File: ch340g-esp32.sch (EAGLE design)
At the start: 0 parts

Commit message: rev1
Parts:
- added C1, C2: 22, rcl:C-EUC0805
- added C3, C5: 0.1uF, rcl:C-EUC0805
- added C4: 10uF, rcl:CPOL-EUB/3528-21W
- added D1: YELLOW, 597-5311-402F:597-5311-402F
- added D2: GREEN, 597-5311-402F:597-5311-402F
- added IC1: LM1117MPX-3.3, lm1117:LM1117MPX-3.3
- added JP1: OUT, pinhead:PINHD-1X6
- added Q1: 12M, crystal:CRYSTALHC49S
- added R1, R2: 10K, rcl:R-EU_R0805
- added R3, R4: 2K, rcl:R-EU_R0805
- added T1, T2: BC847, transistor:BC847
- added U$1: MICRO-USB, microusb:MICRO-USB
- added U$2: CH340G, ch340g:CH340G
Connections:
- new net +5V: C3.1, IC1.IN, U$1.VCC
- new net D+: U$1.D+, U$2.D+
- new net D-: U$1.D-, U$2.D-
- new net DTR: R1.1, T2.E, U$2.DTR
- new net EN: JP1.1, T1.C
- new net GND: C1.2, C2.2, C3.2, C4.-, C5.2, IC1.GND, JP1.6, U$1.GND, U$1.GND@1, U$1.GND@2, U$2.GND
- new net IO0: JP1.2, T2.C
- new net N$1: C2.1, Q1.2, U$2.XO
- new net N$12: D2.A, R4.1
- new net N$2: C1.1, Q1.1, U$2.XI
- new net N$3: R1.2, T1.B
- new net N$4: R2.2, T2.B
- new net N$5: D1.A, R3.1
- new net RTS: R2.1, T1.E, U$2.RTS
- new net RX: D2.C, JP1.3, U$2.RX
- new net TX: D1.C, JP1.4, U$2.TX
- new net VCC: C4.+, C5.1, IC1.OUT, IC1.OUT1, JP1.5, R3.2, R4.2, U$2.V3, U$2.VCC

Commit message: board update
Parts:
- added D3: GREEN, 597-5311-402F:597-5311-402F
- added R5: 2K, rcl:R-EU_R0805
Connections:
- new net N$6: D3.A, R5.1
- net GND: now also D3.C
- net VCC: now also R5.2
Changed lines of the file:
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@@
 <?xml version="1.0" encoding="utf-8"?>
 <!DOCTYPE eagle SYSTEM "eagle.dtd">
-<eagle version="9.4.2">
+<eagle version="9.5.0">
 <drawing>
 <settings>
@@
 <part name="P+9" library="supply1" library_urn="urn:adsk.eagle:library:371" deviceset="VCC" device=""/>
 <part name="GND10" library="supply1" library_urn="urn:adsk.eagle:library:371" deviceset="GND" device=""/>
+<part name="D3" library="597-5311-402F" deviceset="597-5311-402F" device="" value="GREEN"/>
+<part name="R5" library="rcl" library_urn="urn:adsk.eagle:library:334" deviceset="R-EU_" device="R0805" package3d_urn="urn:adsk.eagle:package:23553/2" value="2K"/>
+<part name="P+10" library="supply1" library_urn="urn:adsk.eagle:library:371" deviceset="VCC" device=""/>
+<part name="GND11" library="supply1" library_urn="urn:adsk.eagle:library:371" deviceset="GND" device=""/>
 </parts>
 <sheets>
@@
 <attribute name="VALUE" x="7.62" y="-5.08" size="1.778" layer="96"/>
 </instance>
+<instance part="D3" gate="G$1" x="106.68" y="2.54" smashed="yes" rot="R90">
+<attribute name="NAME" x="102.60973125" y="0.50486875" size="1.780740625" layer="95" rot="R90"/>
+<attribute name="VALUE" x="110.49315" y="0.50631875" size="1.77946875" layer="96" rot="R90"/>
+</instance>
+<instance part="R5" gate="G$1" x="106.68" y="17.78" smashed="yes" rot="R90">
+<attribute name="NAME" x="105.1814" y="13.97" size="1.778" layer="95" rot="R90"/>
+<attribute name="VALUE" x="109.982" y="13.97" size="1.778" layer="96" rot="R90"/>
+</instance>
+<instance part="P+10" gate="VCC" x="106.68" y="25.4" smashed="yes">
+<attribute name="VALUE" x="104.14" y="22.86" size="1.778" layer="96" rot="R90"/>
+</instance>
+<instance part="GND11" gate="1" x="106.68" y="-7.62" smashed="yes">
+<attribute name="VALUE" x="104.14" y="-10.16" size="1.778" layer="96"/>
+</instance>
 </instances>
 <busses>
@@
 <pinref part="C4" gate="G$1" pin="-"/>
 <pinref part="GND10" gate="1" pin="GND"/>
+</segment>
+<segment>
+<pinref part="D3" gate="G$1" pin="C"/>
+<pinref part="GND11" gate="1" pin="GND"/>
 </segment>
 </net>
@@
 <junction x="20.32" y="58.42"/>
 </segment>
-</net>
+<segment>
+<pinref part="R5" gate="G$1" pin="2"/>
+<pinref part="P+10" gate="VCC" pin="VCC"/>
+</segment>
+</net>
+<net name="N$6" class="0">
+<segment>
+<pinref part="D3" gate="G$1" pin="A"/>
+<pinref part="R5" gate="G$1" pin="1"/>
+</segment>
+</net>

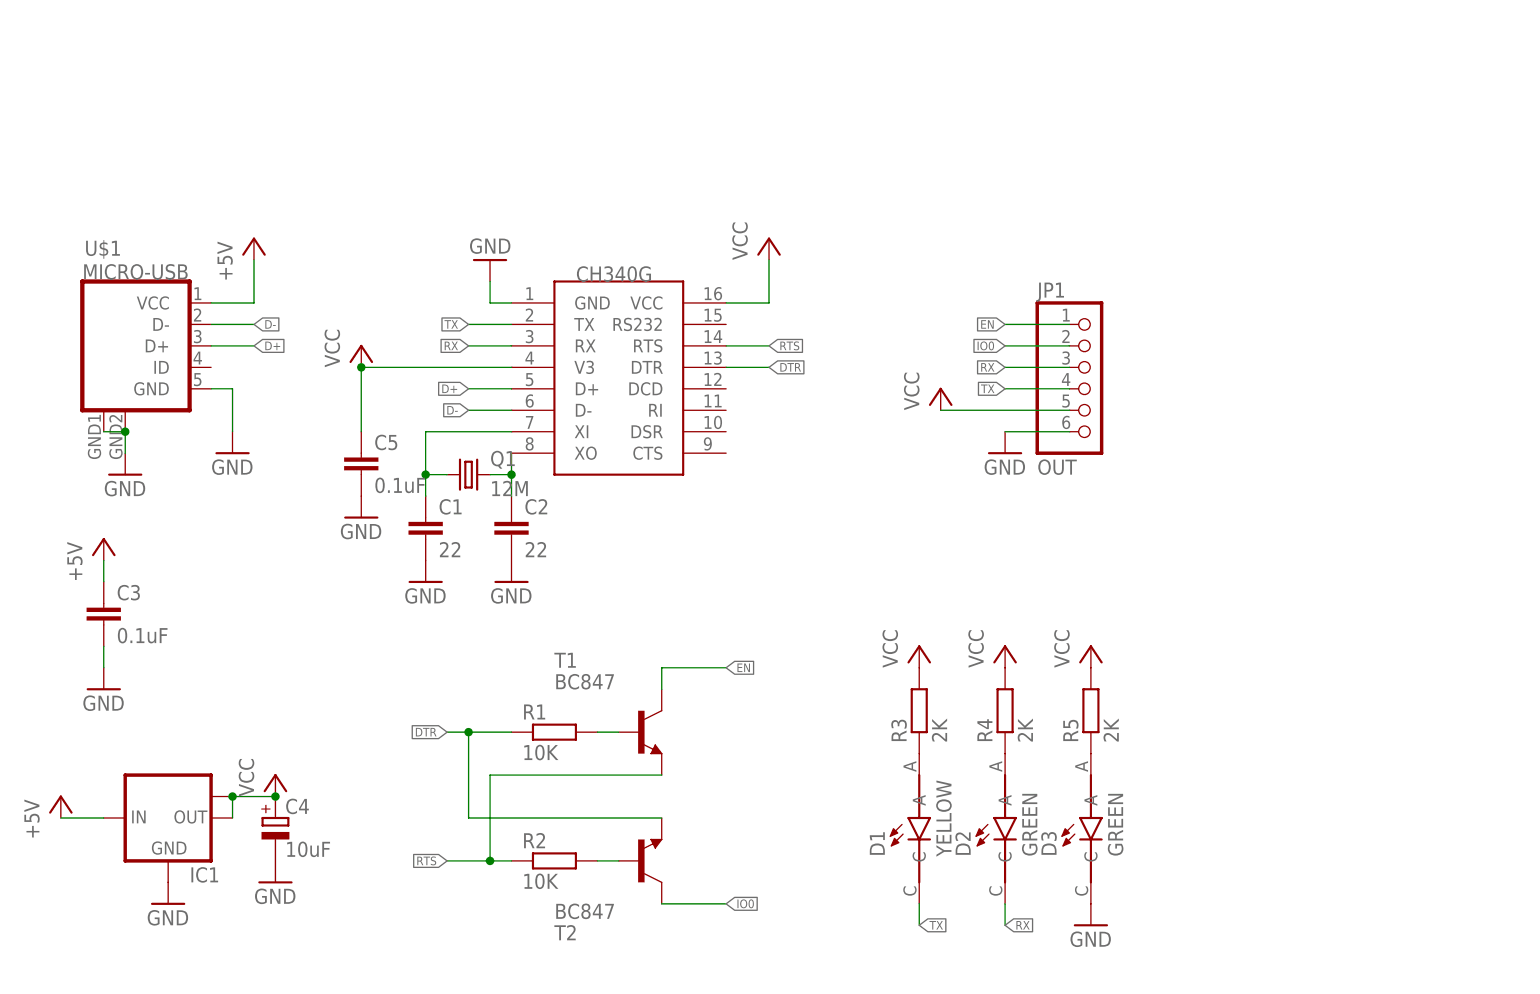
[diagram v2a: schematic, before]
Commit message: USB TypeC connector; Smaller board
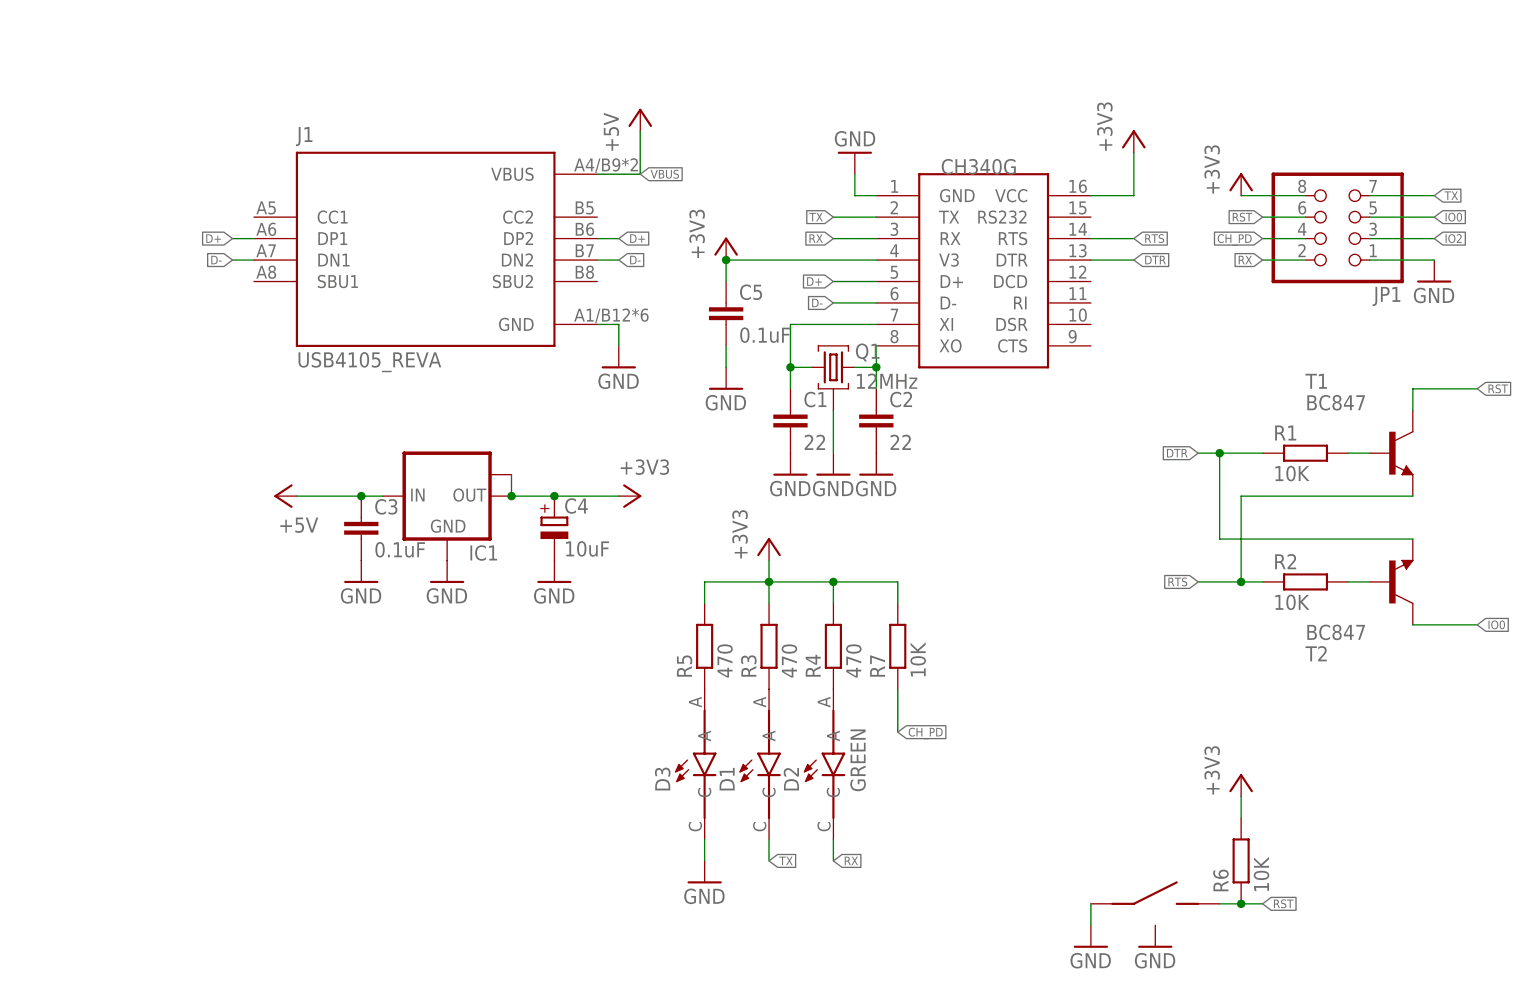
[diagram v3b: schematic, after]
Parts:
- removed U$2: CH340G, ch340g:CH340G
- added J1: USB4105_REVA, USB4105_REVA:USB4105_REVA
- added R6, R7: 10K, rcl:R-EU_R0603
- added U1: CH340G, ch340g:CH340G
- C1, C2, C3, C5: device rcl:C-EUC0805 -> rcl:C-EUC0603
- JP1: value OUT -> (none); device pinhead:PINHD-1X6 -> pinhead:PINHD-2X4
- Q1: value 12M -> 12MHz; device crystal:CRYSTALHC49S -> crystal:YSX321SL
- R1, R2: device rcl:R-EU_R0805 -> rcl:R-EU_R0603
- R3, R4, R5: value 2K -> 470; device rcl:R-EU_R0805 -> rcl:R-EU_R0603
- U$1: value MICRO-USB -> TS36CA-0.7; device microusb:MICRO-USB -> SMD Tact:TS36CA-0.7
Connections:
- removed net +5V: C3.1, IC1.IN, U$1.VCC
- removed net EN: JP1.1, T1.C
- removed net VCC: C4.+, C5.1, IC1.OUT, IC1.OUT1, JP1.5, R3.2, R4.2, R5.2, U$2.V3, U$2.VCC
- new net +3V3: C4.+, C5.1, IC1.OUT, IC1.OUT1, JP1.8, R3.2, R4.2, R5.2, R6.2, R7.2, U1.V3, U1.VCC
- new net CH_PD: JP1.4, R7.1
- new net IO2: JP1.3
- new net RST: JP1.6, R6.1, T1.C, U$1.P$2
- new net VBUS: C3.1, IC1.IN, J1.VBUS
- net D+: now also J1.DP1, J1.DP2, U1.D+; no longer U$1.D+, U$2.D+
- net D-: now also J1.DN1, J1.DN2, U1.D-; no longer U$1.D-, U$2.D-
- net DTR: now also U1.DTR; no longer U$2.DTR
- net GND: now also J1.GND, JP1.1, Q1.CASE, U$1.CASE, U$1.P$1, U1.GND; no longer JP1.6, U$1.GND, U$1.GND@1, U$1.GND@2, U$2.GND
- net IO0: now also JP1.5; no longer JP1.2
- net N$1: now also U1.XO; no longer U$2.XO
- net N$2: now also U1.XI; no longer U$2.XI
- net RTS: now also U1.RTS; no longer U$2.RTS
- net RX: now also JP1.2, U1.RX; no longer JP1.3, U$2.RX
- net TX: now also JP1.7, U1.TX; no longer JP1.4, U$2.TX
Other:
- moved on the sheet: C1, C2, C3, C4, C5, D1, D2, D3, IC1, R1, R2, R3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

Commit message: Production files
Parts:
- removed U$1: TS36CA-0.7, SMD Tact:TS36CA-0.7
- added BTN1: TS36CA-0.7, SMD Tact:TS36CA-0.7
- C3, C5: value 0.1uF -> 10u
- C4: value 10uF -> 100u
- D1: value YELLOW -> BLUE
- D2: value GREEN -> BLUE
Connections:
- net GND: now also BTN1.CASE, BTN1.P$1; no longer U$1.CASE, U$1.P$1
- net RST: now also BTN1.P$2; no longer U$1.P$2
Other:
- moved on the sheet: R6
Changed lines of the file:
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@@
 <part name="GND5" library="supply1" library_urn="urn:adsk.eagle:library:371" deviceset="GND" device=""/>
 <part name="R2" library="rcl" library_urn="urn:adsk.eagle:library:334" deviceset="R-EU_" device="R0603" package3d_urn="urn:adsk.eagle:package:23555/3" value="10K"/>
-<part name="D1" library="597-5311-402F" deviceset="597-5311-402F" device="" value="YELLOW"/>
-<part name="C3" library="rcl" library_urn="urn:adsk.eagle:library:334" deviceset="C-EU" device="C0603" package3d_urn="urn:adsk.eagle:package:23616/2" value="0.1uF"/>
+<part name="D1" library="597-5311-402F" deviceset="597-5311-402F" device="" value="BLUE"/>
+<part name="C3" library="rcl" library_urn="urn:adsk.eagle:library:334" deviceset="C-EU" device="C0603" package3d_urn="urn:adsk.eagle:package:23616/2" value="10u"/>
 <part name="GND6" library="supply1" library_urn="urn:adsk.eagle:library:371" deviceset="GND" device=""/>
-<part name="C4" library="rcl" library_urn="urn:adsk.eagle:library:334" deviceset="CPOL-EU" device="B/3528-21W" package3d_urn="urn:adsk.eagle:package:23411/1" value="10uF"/>
+<part name="C4" library="rcl" library_urn="urn:adsk.eagle:library:334" deviceset="CPOL-EU" device="B/3528-21W" package3d_urn="urn:adsk.eagle:package:23411/1" value="100u"/>
 <part name="GND7" library="supply1" library_urn="urn:adsk.eagle:library:371" deviceset="GND" device=""/>
 <part name="R3" library="rcl" library_urn="urn:adsk.eagle:library:334" deviceset="R-EU_" device="R0603" package3d_urn="urn:adsk.eagle:package:23555/3" value="470"/>
-<part name="C5" library="rcl" library_urn="urn:adsk.eagle:library:334" deviceset="C-EU" device="C0603" package3d_urn="urn:adsk.eagle:package:23616/2" value="0.1uF"/>
+<part name="C5" library="rcl" library_urn="urn:adsk.eagle:library:334" deviceset="C-EU" device="C0603" package3d_urn="urn:adsk.eagle:package:23616/2" value="10u"/>
 <part name="GND8" library="supply1" library_urn="urn:adsk.eagle:library:371" deviceset="GND" device=""/>
-<part name="D2" library="597-5311-402F" deviceset="597-5311-402F" device="" value="GREEN"/>
+<part name="D2" library="597-5311-402F" deviceset="597-5311-402F" device="" value="BLUE"/>
 <part name="R4" library="rcl" library_urn="urn:adsk.eagle:library:334" deviceset="R-EU_" device="R0603" package3d_urn="urn:adsk.eagle:package:23555/3" value="470"/>
 <part name="IC1" library="lm1117" deviceset="LM1117MPX-*" device="" technology="3.3" value=""/>
@@
 <part name="R7" library="rcl" library_urn="urn:adsk.eagle:library:334" deviceset="R-EU_" device="R0603" package3d_urn="urn:adsk.eagle:package:23555/3" value="10K"/>
 <part name="P+3" library="supply1" library_urn="urn:adsk.eagle:library:371" deviceset="+3V3" device=""/>
-<part name="U$1" library="SMD Tact" deviceset="TS36CA-0.7" device=""/>
+<part name="BTN1" library="SMD Tact" deviceset="TS36CA-0.7" device=""/>
 <part name="GND1" library="supply1" library_urn="urn:adsk.eagle:library:371" deviceset="GND" device=""/>
 <part name="GND13" library="supply1" library_urn="urn:adsk.eagle:library:371" deviceset="GND" device=""/>
@@
 <attribute name="VALUE" x="73.66" y="43.18" size="1.778" layer="96"/>
 </instance>
-<instance part="R6" gate="G$1" x="124.46" y="0" smashed="yes" rot="R90">
-<attribute name="NAME" x="122.9614" y="-3.81" size="1.778" layer="95" rot="R90"/>
-<attribute name="VALUE" x="127.762" y="-3.81" size="1.778" layer="96" rot="R90"/>
+<instance part="R6" gate="G$1" x="116.84" y="10.16" smashed="yes" rot="R90">
+<attribute name="NAME" x="115.3414" y="6.35" size="1.778" layer="95" rot="R90"/>
+<attribute name="VALUE" x="120.142" y="6.35" size="1.778" layer="96" rot="R90"/>
 </instance>
 <instance part="R7" gate="G$1" x="83.82" y="25.4" smashed="yes" rot="R90">
@@
 <attribute name="VALUE" x="87.122" y="21.59" size="1.778" layer="96" rot="R90"/>
 </instance>
-<instance part="P+3" gate="G$1" x="124.46" y="10.16" smashed="yes">
-<attribute name="VALUE" x="121.92" y="7.62" size="1.778" layer="96" rot="R90"/>
-</instance>
-<instance part="U$1" gate="G$1" x="114.3" y="-5.08" smashed="yes"/>
-<instance part="GND1" gate="1" x="106.68" y="-10.16" smashed="yes">
-<attribute name="VALUE" x="104.14" y="-12.7" size="1.778" layer="96"/>
-</instance>
-<instance part="GND13" gate="1" x="114.3" y="-10.16" smashed="yes">
-<attribute name="VALUE" x="111.76" y="-12.7" size="1.778" layer="96"/>
+<instance part="P+3" gate="G$1" x="116.84" y="20.32" smashed="yes">
+<attribute name="VALUE" x="114.3" y="17.78" size="1.778" layer="96" rot="R90"/>
+</instance>
+<instance part="BTN1" gate="G$1" x="106.68" y="5.08" smashed="yes"/>
+<instance part="GND1" gate="1" x="99.06" y="0" smashed="yes">
+<attribute name="VALUE" x="96.52" y="-2.54" size="1.778" layer="96"/>
+</instance>
+<instance part="GND13" gate="1" x="106.68" y="0" smashed="yes">
+<attribute name="VALUE" x="104.14" y="-2.54" size="1.778" layer="96"/>
 </instance>
 </instances>
@@
 </segment>
 <segment>
-<pinref part="U$1" gate="G$1" pin="P$1"/>
+<pinref part="BTN1" gate="G$1" pin="P$1"/>
 <pinref part="GND1" gate="1" pin="GND"/>
-<wire x1="106.68" y1="-7.62" x2="106.68" y2="-5.08" width="0.1524" layer="91"/>
-</segment>
-<segment>
-<pinref part="U$1" gate="G$1" pin="CASE"/>
+<wire x1="99.06" y1="2.54" x2="99.06" y2="5.08" width="0.1524" layer="91"/>
+</segment>
+<segment>
+<pinref part="BTN1" gate="G$1" pin="CASE"/>
 <pinref part="GND13" gate="1" pin="GND"/>
 </segment>
@@
 <pinref part="R6" gate="G$1" pin="2"/>
 <pinref part="P+3" gate="G$1" pin="+3V3"/>
-<wire x1="124.46" y1="5.08" x2="124.46" y2="7.62" width="0.1524" layer="91"/>
+<wire x1="116.84" y1="15.24" x2="116.84" y2="17.78" width="0.1524" layer="91"/>
 </segment>
 </net>
@@
 </segment>
 <segment>
-<pinref part="U$1" gate="G$1" pin="P$2"/>
+<pinref part="BTN1" gate="G$1" pin="P$2"/>
 <pinref part="R6" gate="G$1" pin="1"/>
-<wire x1="124.46" y1="-5.08" x2="121.92" y2="-5.08" width="0.1524" layer="91"/>
-<wire x1="124.46" y1="-5.08" x2="127" y2="-5.08" width="0.1524" layer="91"/>
-<junction x="124.46" y="-5.08"/>
-<label x="127" y="-5.08" size="1.016" layer="95" xref="yes"/>
-</segment>
-</net>
+<wire x1="116.84" y1="5.08" x2="114.3" y2="5.08" width="0.1524" layer="91"/>
+<wire x1="116.84" y1="5.08" x2="119.38" y2="5.08" width="0.1524" layer="91"/>
+<junction x="116.84" y="5.08"/>
+<label x="119.38" y="5.08" size="1.016" layer="95" xref="yes"/>
+</segment>
+</net>

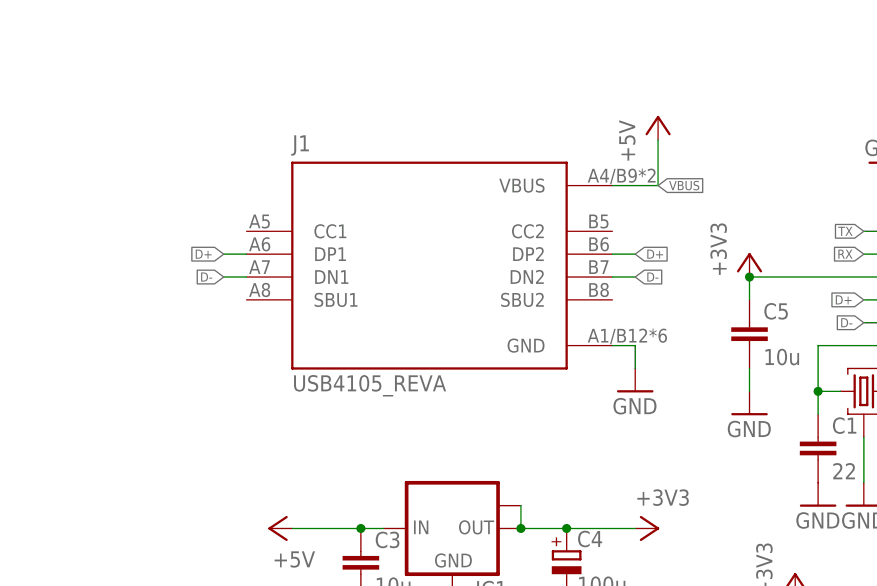
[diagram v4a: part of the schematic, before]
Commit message: Added support for powering from USB Cable
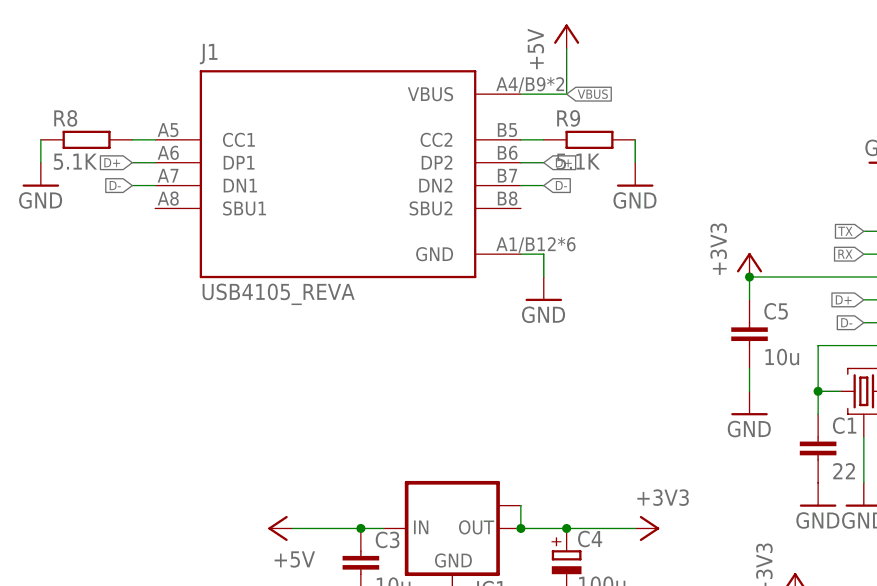
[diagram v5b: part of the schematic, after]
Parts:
- added R8, R9: 5.1K, rcl:R-EU_R0603
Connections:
- new net N$7: J1.CC1, R8.2
- new net N$8: J1.CC2, R9.1
- net GND: now also R8.1, R9.2
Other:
- moved on the sheet: J1
